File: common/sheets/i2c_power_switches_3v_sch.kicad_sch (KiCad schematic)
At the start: 7 parts, among them U17 MCP23008T-E/SS, U18 INA226

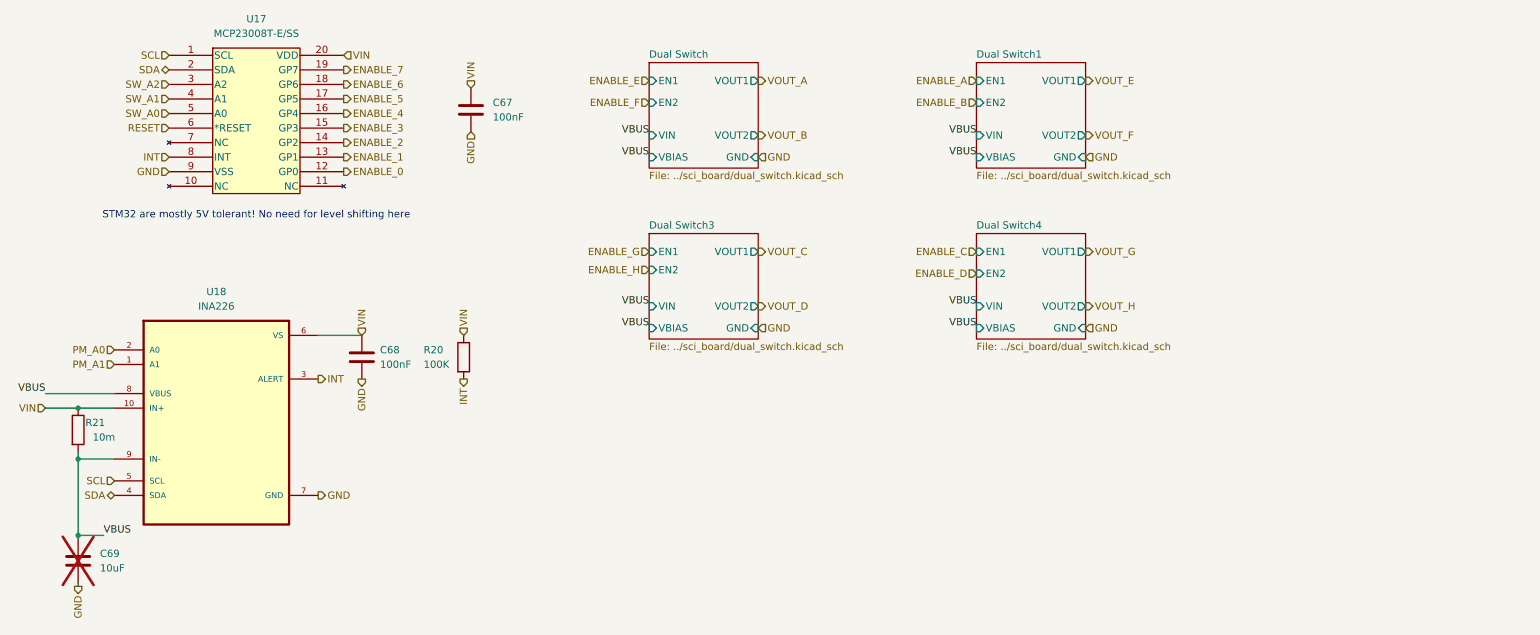
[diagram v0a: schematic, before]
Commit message: absolute paths for includes of includes or the second level common/sheet will cause problems!
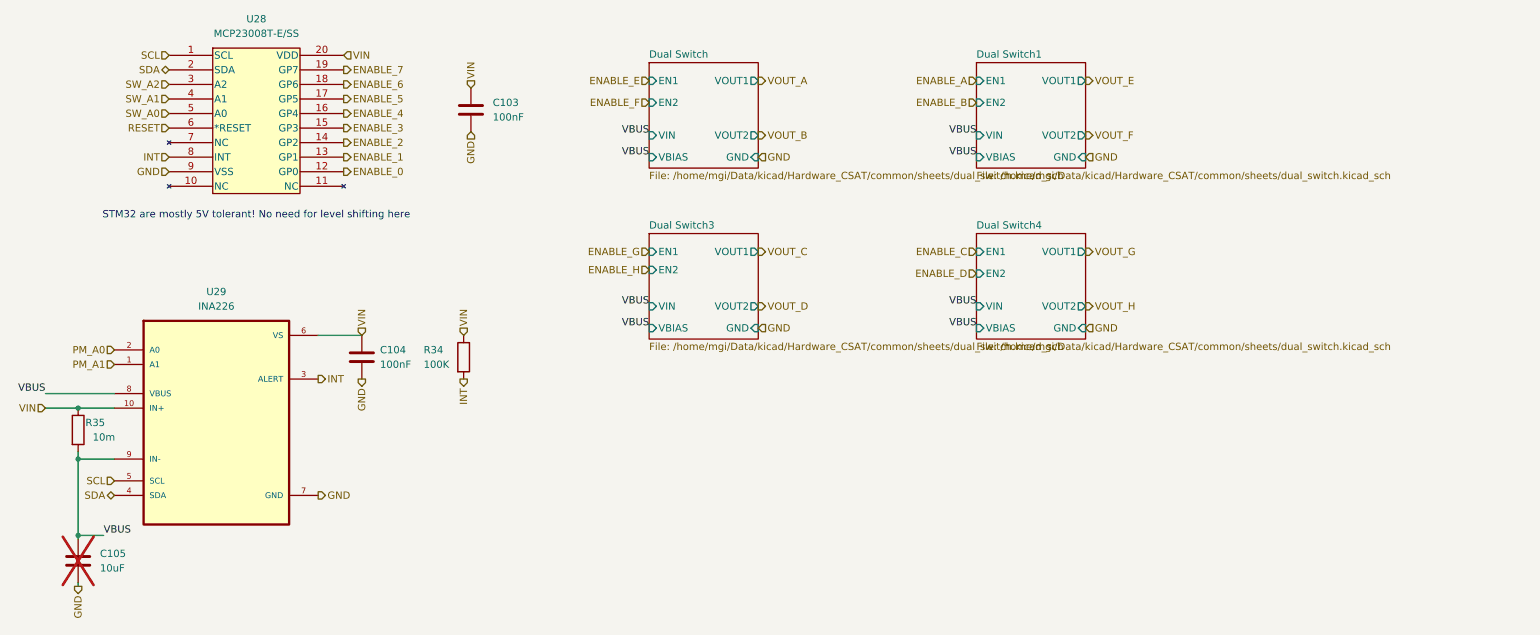
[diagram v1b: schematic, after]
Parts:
- renumbered C67 to C103, C68 to C104, C69 to C105, R20 to R34, R21 to R35, U17 to U28, U18 to U29
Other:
- sheet Dual Switch: file ../sci_board/dual_switch.kicad_sch -> /home/mgi/Data/kicad/Hardware_CSAT/common/sheets/dual_switch.kicad_sch
- sheet Dual Switch1: file ../sci_board/dual_switch.kicad_sch -> /home/mgi/Data/kicad/Hardware_CSAT/common/sheets/dual_switch.kicad_sch
- sheet Dual Switch3: file ../sci_board/dual_switch.kicad_sch -> /home/mgi/Data/kicad/Hardware_CSAT/common/sheets/dual_switch.kicad_sch
- sheet Dual Switch4: file ../sci_board/dual_switch.kicad_sch -> /home/mgi/Data/kicad/Hardware_CSAT/common/sheets/dual_switch.kicad_sch
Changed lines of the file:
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@@
 		(on_board yes)
 		(dnp no)
-		(property "Reference" "R21"
+		(property "Reference" "R35"
 			(at 38.1 99.06 0)
 			(effects
@@
 			(project "EPS"
 				(path "/05170af6-30ef-4c3a-b972-f098085da1bc/365e30aa-57e3-49e2-b136-6964bfe03313"
-					(reference "R34")
+					(reference "R35")
+					(unit 1)
+				)
+			)
+			(project "i2c_power_switches_3v_sch"
+				(path "/4a0b4739-c903-4b91-9f8d-5a4aa8b4f74d"
+					(reference "R?")
 					(unit 1)
 				)
@@
 		(on_board yes)
 		(dnp no)
-		(property "Reference" "R20"
+		(property "Reference" "R34"
 			(at 97.155 86.36 0)
 			(effects
@@
 			(project "EPS"
 				(path "/05170af6-30ef-4c3a-b972-f098085da1bc/365e30aa-57e3-49e2-b136-6964bfe03313"
-					(reference "R33")
+					(reference "R34")
+					(unit 1)
+				)
+			)
+			(project "i2c_power_switches_3v_sch"
+				(path "/4a0b4739-c903-4b91-9f8d-5a4aa8b4f74d"
+					(reference "R?")
 					(unit 1)
 				)
@@
 		(dnp no)
 		(fields_autoplaced yes)
-		(property "Reference" "U17"
+		(property "Reference" "U28"
 			(at 67.945 28.575 0)
 			(effects
@@
 			(project "EPS"
 				(path "/05170af6-30ef-4c3a-b972-f098085da1bc/365e30aa-57e3-49e2-b136-6964bfe03313"
-					(reference "U22")
+					(reference "U28")
+					(unit 1)
+				)
+			)
+			(project "i2c_power_switches_3v_sch"
+				(path "/4a0b4739-c903-4b91-9f8d-5a4aa8b4f74d"
+					(reference "U?")
 					(unit 1)
 				)
@@
 		(dnp no)
 		(fields_autoplaced yes)
-		(property "Reference" "C68"
+		(property "Reference" "C104"
 			(at 89.535 86.3599 0)
 			(effects
@@
 			(project "EPS"
 				(path "/05170af6-30ef-4c3a-b972-f098085da1bc/365e30aa-57e3-49e2-b136-6964bfe03313"
-					(reference "C68")
+					(reference "C104")
+					(unit 1)
+				)
+			)
+			(project "i2c_power_switches_3v_sch"
+				(path "/4a0b4739-c903-4b91-9f8d-5a4aa8b4f74d"
+					(reference "C?")
 					(unit 1)
 				)
@@
 		(dnp no)
 		(fields_autoplaced yes)
-		(property "Reference" "C67"
+		(property "Reference" "C103"
 			(at 109.22 43.1799 0)
 			(effects
@@
 			(project "EPS"
 				(path "/05170af6-30ef-4c3a-b972-f098085da1bc/365e30aa-57e3-49e2-b136-6964bfe03313"
-					(reference "C67")
+					(reference "C103")
+					(unit 1)
+				)
+			)
+			(project "i2c_power_switches_3v_sch"
+				(path "/4a0b4739-c903-4b91-9f8d-5a4aa8b4f74d"
+					(reference "C?")
 					(unit 1)
 				)
@@
 		(dnp yes)
 		(fields_autoplaced yes)
-		(property "Reference" "C69"
+		(property "Reference" "C105"
 			(at 40.64 121.9199 0)
 			(effects
@@
 			(project "EPS"
 				(path "/05170af6-30ef-4c3a-b972-f098085da1bc/365e30aa-57e3-49e2-b136-6964bfe03313"
-					(reference "C69")
+					(reference "C105")
+					(unit 1)
+				)
+			)
+			(project "i2c_power_switches_3v_sch"
+				(path "/4a0b4739-c903-4b91-9f8d-5a4aa8b4f74d"
+					(reference "C?")
 					(unit 1)
 				)
@@
 		(dnp no)
 		(fields_autoplaced yes)
-		(property "Reference" "U18"
+		(property "Reference" "U29"
 			(at 60.96 76.2 0)
 			(effects
@@
 			(project "EPS"
 				(path "/05170af6-30ef-4c3a-b972-f098085da1bc/365e30aa-57e3-49e2-b136-6964bfe03313"
-					(reference "U23")
+					(reference "U29")
+					(unit 1)
+				)
+			)
+			(project "i2c_power_switches_3v_sch"
+				(path "/4a0b4739-c903-4b91-9f8d-5a4aa8b4f74d"
+					(reference "U?")
 					(unit 1)
 				)
@@
 			)
 		)
-		(property "Sheetfile" "../sci_board/dual_switch.kicad_sch"
+		(property "Sheetfile" "/home/mgi/Data/kicad/Hardware_CSAT/common/sheets/dual_switch.kicad_sch"
 			(at 136.525 55.1946 0)
 			(effects
@@
 				(path "/f6cc00ab-17f1-4973-862f-7ac95fe70668/6161e047-2bb5-4856-b93a-088a3805633f"
 					(page "37")
+				)
+			)
+			(project "EPS"
+				(path "/05170af6-30ef-4c3a-b972-f098085da1bc/365e30aa-57e3-49e2-b136-6964bfe03313"
+					(page "#")
+				)
+			)
+			(project "i2c_power_switches_3v_sch"
+				(path "/4a0b4739-c903-4b91-9f8d-5a4aa8b4f74d"
+					(page "2")
 				)
 			)
@@
 			)
 		)
-		(property "Sheetfile" "../sci_board/dual_switch.kicad_sch"
+		(property "Sheetfile" "/home/mgi/Data/kicad/Hardware_CSAT/common/sheets/dual_switch.kicad_sch"
 			(at 136.525 85.0396 0)
 			(effects
@@
 				(path "/f6cc00ab-17f1-4973-862f-7ac95fe70668/6161e047-2bb5-4856-b93a-088a3805633f"
 					(page "39")
+				)
+			)
+			(project "EPS"
+				(path "/05170af6-30ef-4c3a-b972-f098085da1bc/365e30aa-57e3-49e2-b136-6964bfe03313"
+					(page "#")
+				)
+			)
+			(project "i2c_power_switches_3v_sch"
+				(path "/4a0b4739-c903-4b91-9f8d-5a4aa8b4f74d"
+					(page "3")
 				)
 			)
@@
 			)
 		)
-		(property "Sheetfile" "../sci_board/dual_switch.kicad_sch"
+		(property "Sheetfile" "/home/mgi/Data/kicad/Hardware_CSAT/common/sheets/dual_switch.kicad_sch"
 			(at 193.675 55.1946 0)
 			(effects
@@
 				(path "/f6cc00ab-17f1-4973-862f-7ac95fe70668/6161e047-2bb5-4856-b93a-088a3805633f"
 					(page "40")
+				)
+			)
+			(project "EPS"
+				(path "/05170af6-30ef-4c3a-b972-f098085da1bc/365e30aa-57e3-49e2-b136-6964bfe03313"
+					(page "#")
+				)
+			)
+			(project "i2c_power_switches_3v_sch"
+				(path "/4a0b4739-c903-4b91-9f8d-5a4aa8b4f74d"
+					(page "4")
 				)
 			)
@@
 			)
 		)
-		(property "Sheetfile" "../sci_board/dual_switch.kicad_sch"
+		(property "Sheetfile" "/home/mgi/Data/kicad/Hardware_CSAT/common/sheets/dual_switch.kicad_sch"
 			(at 193.675 85.0396 0)
 			(effects
@@
 				)
 			)
+			(project "EPS"
+				(path "/05170af6-30ef-4c3a-b972-f098085da1bc/365e30aa-57e3-49e2-b136-6964bfe03313"
+					(page "#")
+				)
+			)
+			(project "i2c_power_switches_3v_sch"
+				(path "/4a0b4739-c903-4b91-9f8d-5a4aa8b4f74d"
+					(page "5")
+				)
+			)

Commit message: move legacy schema and files into inactive folders for removal
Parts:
- renumbered C103 to C67, C104 to C68, C105 to C69, R34 to R20, R35 to R21, U28 to U17, U29 to U18
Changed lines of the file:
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@@
 		(on_board yes)
 		(dnp no)
-		(property "Reference" "R35"
+		(property "Reference" "R21"
 			(at 38.1 99.06 0)
 			(effects
@@
 		(on_board yes)
 		(dnp no)
-		(property "Reference" "R34"
+		(property "Reference" "R20"
 			(at 97.155 86.36 0)
 			(effects
@@
 		(dnp no)
 		(fields_autoplaced yes)
-		(property "Reference" "U28"
+		(property "Reference" "U17"
 			(at 67.945 28.575 0)
 			(effects
@@
 		(dnp no)
 		(fields_autoplaced yes)
-		(property "Reference" "C104"
+		(property "Reference" "C68"
 			(at 89.535 86.3599 0)
 			(effects
@@
 		(dnp no)
 		(fields_autoplaced yes)
-		(property "Reference" "C103"
+		(property "Reference" "C67"
 			(at 109.22 43.1799 0)
 			(effects
@@
 		(dnp yes)
 		(fields_autoplaced yes)
-		(property "Reference" "C105"
+		(property "Reference" "C69"
 			(at 40.64 121.9199 0)
 			(effects
@@
 		(dnp no)
 		(fields_autoplaced yes)
-		(property "Reference" "U29"
+		(property "Reference" "U18"
 			(at 60.96 76.2 0)
 			(effects

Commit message: cleaning up common sheets and projects. prepare for removal of legacy path links
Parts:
- renumbered C67 to C103, C68 to C104, C69 to C105, R20 to R34, R21 to R35, U17 to U28, U18 to U29
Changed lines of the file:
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@@
 		(on_board yes)
 		(dnp no)
-		(property "Reference" "R21"
+		(property "Reference" "R35"
 			(at 38.1 99.06 0)
 			(effects
@@
 		(on_board yes)
 		(dnp no)
-		(property "Reference" "R20"
+		(property "Reference" "R34"
 			(at 97.155 86.36 0)
 			(effects
@@
 		(dnp no)
 		(fields_autoplaced yes)
-		(property "Reference" "U17"
+		(property "Reference" "U28"
 			(at 67.945 28.575 0)
 			(effects
@@
 		(dnp no)
 		(fields_autoplaced yes)
-		(property "Reference" "C68"
+		(property "Reference" "C104"
 			(at 89.535 86.3599 0)
 			(effects
@@
 		(dnp no)
 		(fields_autoplaced yes)
-		(property "Reference" "C67"
+		(property "Reference" "C103"
 			(at 109.22 43.1799 0)
 			(effects
@@
 		(dnp yes)
 		(fields_autoplaced yes)
-		(property "Reference" "C69"
+		(property "Reference" "C105"
 			(at 40.64 121.9199 0)
 			(effects
@@
 		(dnp no)
 		(fields_autoplaced yes)
-		(property "Reference" "U18"
+		(property "Reference" "U29"
 			(at 60.96 76.2 0)
 			(effects
